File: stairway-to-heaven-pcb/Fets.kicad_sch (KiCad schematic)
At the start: 7 parts, among them J14 Conn_01x04_Male, Q40 FDN337N, Q41 FDN337N, Q42 FDN337N

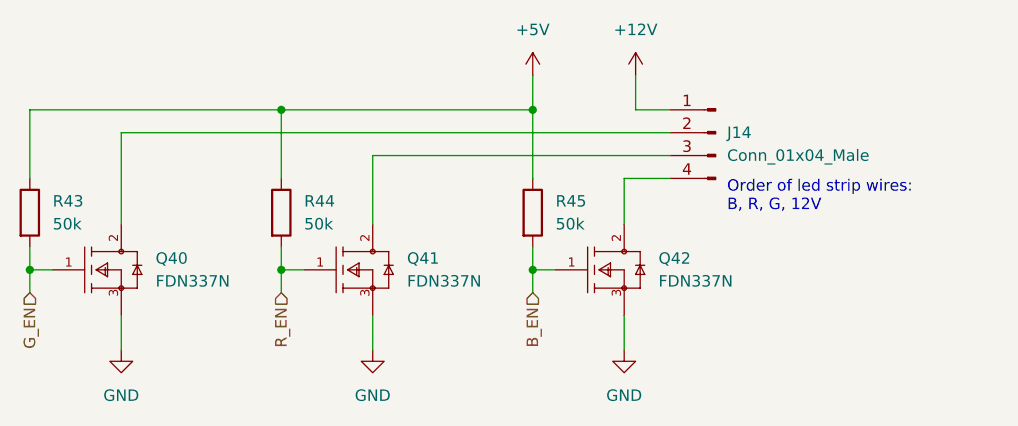
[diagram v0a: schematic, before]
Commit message: Add sensor drawing
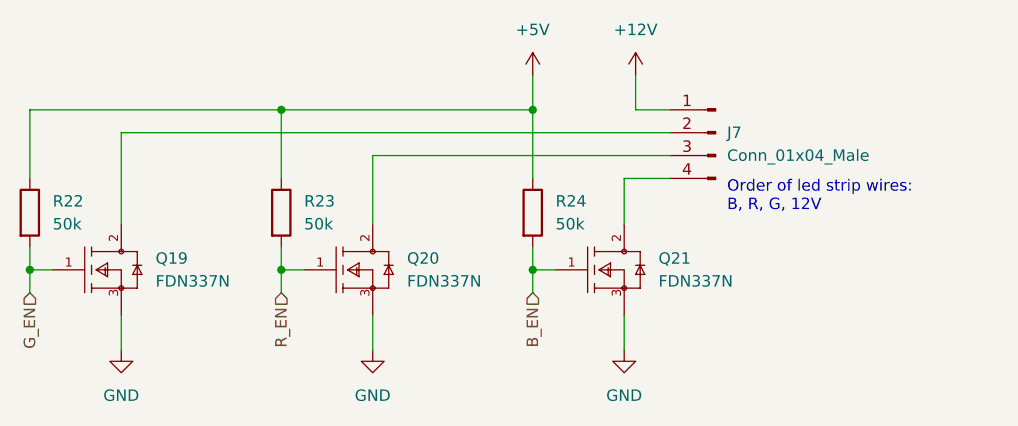
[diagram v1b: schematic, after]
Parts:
- renumbered J14 to J7, Q40 to Q19, Q41 to Q20, Q42 to Q21, R43 to R22, R44 to R23, R45 to R24
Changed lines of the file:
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@@
   (symbol (lib_id "Device:R") (at 96.52 99.06 0)
     (in_bom yes) (on_board yes) (fields_autoplaced)
-    (property "Reference" "R43" (id 0) (at 99.06 97.7899 0)
+    (property "Reference" "R22" (id 0) (at 99.06 97.7899 0)
       (effects (font (size 1.27 1.27)) (justify left))
     )
@@
   (symbol (lib_id "power:GND") (at 162.56 114.3 0)
     (in_bom yes) (on_board yes) (fields_autoplaced)
-    (property "Reference" "#PWR0157" (id 0) (at 162.56 120.65 0)
+    (property "Reference" "#PWR0129" (id 0) (at 162.56 120.65 0)
       (effects (font (size 1.27 1.27)) hide)
     )
@@
   (symbol (lib_id "FDN337N:FDN337N") (at 96.52 105.41 0)
     (in_bom yes) (on_board yes) (fields_autoplaced)
-    (property "Reference" "Q40" (id 0) (at 110.49 104.1399 0)
+    (property "Reference" "Q19" (id 0) (at 110.49 104.1399 0)
       (effects (font (size 1.27 1.27)) (justify left))
     )
@@
   (symbol (lib_id "FDN337N:FDN337N") (at 152.4 105.41 0)
     (in_bom yes) (on_board yes) (fields_autoplaced)
-    (property "Reference" "Q42" (id 0) (at 166.37 104.1399 0)
+    (property "Reference" "Q21" (id 0) (at 166.37 104.1399 0)
       (effects (font (size 1.27 1.27)) (justify left))
     )
@@
   (symbol (lib_id "power:GND") (at 134.62 114.3 0)
     (in_bom yes) (on_board yes) (fields_autoplaced)
-    (property "Reference" "#PWR0155" (id 0) (at 134.62 120.65 0)
+    (property "Reference" "#PWR0127" (id 0) (at 134.62 120.65 0)
       (effects (font (size 1.27 1.27)) hide)
     )
@@
   (symbol (lib_id "Connector:Conn_01x04_Male") (at 172.72 90.17 0) (mirror y)
     (in_bom yes) (on_board yes) (fields_autoplaced)
-    (property "Reference" "J14" (id 0) (at 173.99 90.1699 0)
+    (property "Reference" "J7" (id 0) (at 173.99 90.1699 0)
       (effects (font (size 1.27 1.27)) (justify right))
     )
@@
   (symbol (lib_id "FDN337N:FDN337N") (at 124.46 105.41 0)
     (in_bom yes) (on_board yes) (fields_autoplaced)
-    (property "Reference" "Q41" (id 0) (at 138.43 104.1399 0)
+    (property "Reference" "Q20" (id 0) (at 138.43 104.1399 0)
       (effects (font (size 1.27 1.27)) (justify left))
     )
@@
   (symbol (lib_id "power:+5V") (at 152.4 83.82 0)
     (in_bom yes) (on_board yes) (fields_autoplaced)
-    (property "Reference" "#PWR0179" (id 0) (at 152.4 87.63 0)
+    (property "Reference" "#PWR0172" (id 0) (at 152.4 87.63 0)
       (effects (font (size 1.27 1.27)) hide)
     )
@@
   (symbol (lib_id "power:GND") (at 106.68 114.3 0)
     (in_bom yes) (on_board yes) (fields_autoplaced)
-    (property "Reference" "#PWR0156" (id 0) (at 106.68 120.65 0)
+    (property "Reference" "#PWR0128" (id 0) (at 106.68 120.65 0)
       (effects (font (size 1.27 1.27)) hide)
     )
@@
   (symbol (lib_id "power:+12V") (at 163.83 83.82 0)
     (in_bom yes) (on_board yes) (fields_autoplaced)
-    (property "Reference" "#PWR0158" (id 0) (at 163.83 87.63 0)
+    (property "Reference" "#PWR0130" (id 0) (at 163.83 87.63 0)
       (effects (font (size 1.27 1.27)) hide)
     )
@@
   (symbol (lib_id "Device:R") (at 152.4 99.06 0)
     (in_bom yes) (on_board yes) (fields_autoplaced)
-    (property "Reference" "R45" (id 0) (at 154.94 97.7899 0)
+    (property "Reference" "R24" (id 0) (at 154.94 97.7899 0)
       (effects (font (size 1.27 1.27)) (justify left))
     )
@@
   (symbol (lib_id "Device:R") (at 124.46 99.06 0)
     (in_bom yes) (on_board yes) (fields_autoplaced)
-    (property "Reference" "R44" (id 0) (at 127 97.7899 0)
-      (effects (font (size 1.27 1.27)) (justify left))
-    )
+    (property "Reference" "R23" (id 0) (at 127 97.7899 0)
+      (effects (font (size 1.27 1.27)) (justify left))
+    )

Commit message: Add terminal for sensors
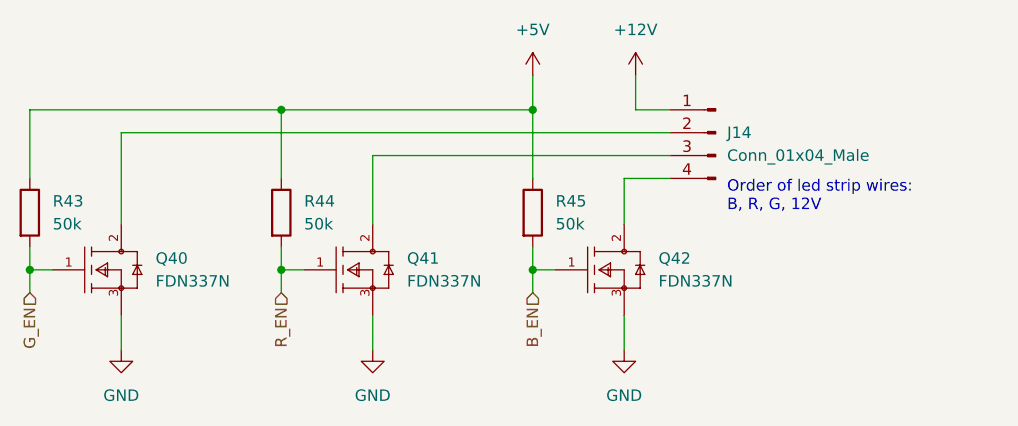
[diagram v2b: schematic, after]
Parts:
- renumbered J7 to J14, Q19 to Q40, Q20 to Q41, Q21 to Q42, R22 to R43, R23 to R44, R24 to R45
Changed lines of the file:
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@@
   (symbol (lib_id "Device:R") (at 96.52 99.06 0)
     (in_bom yes) (on_board yes) (fields_autoplaced)
-    (property "Reference" "R22" (id 0) (at 99.06 97.7899 0)
+    (property "Reference" "R43" (id 0) (at 99.06 97.7899 0)
       (effects (font (size 1.27 1.27)) (justify left))
     )
@@
   (symbol (lib_id "power:GND") (at 162.56 114.3 0)
     (in_bom yes) (on_board yes) (fields_autoplaced)
-    (property "Reference" "#PWR0129" (id 0) (at 162.56 120.65 0)
+    (property "Reference" "#PWR0157" (id 0) (at 162.56 120.65 0)
       (effects (font (size 1.27 1.27)) hide)
     )
@@
   (symbol (lib_id "FDN337N:FDN337N") (at 96.52 105.41 0)
     (in_bom yes) (on_board yes) (fields_autoplaced)
-    (property "Reference" "Q19" (id 0) (at 110.49 104.1399 0)
+    (property "Reference" "Q40" (id 0) (at 110.49 104.1399 0)
       (effects (font (size 1.27 1.27)) (justify left))
     )
@@
   (symbol (lib_id "FDN337N:FDN337N") (at 152.4 105.41 0)
     (in_bom yes) (on_board yes) (fields_autoplaced)
-    (property "Reference" "Q21" (id 0) (at 166.37 104.1399 0)
+    (property "Reference" "Q42" (id 0) (at 166.37 104.1399 0)
       (effects (font (size 1.27 1.27)) (justify left))
     )
@@
   (symbol (lib_id "power:GND") (at 134.62 114.3 0)
     (in_bom yes) (on_board yes) (fields_autoplaced)
-    (property "Reference" "#PWR0127" (id 0) (at 134.62 120.65 0)
+    (property "Reference" "#PWR0155" (id 0) (at 134.62 120.65 0)
       (effects (font (size 1.27 1.27)) hide)
     )
@@
   (symbol (lib_id "Connector:Conn_01x04_Male") (at 172.72 90.17 0) (mirror y)
     (in_bom yes) (on_board yes) (fields_autoplaced)
-    (property "Reference" "J7" (id 0) (at 173.99 90.1699 0)
+    (property "Reference" "J14" (id 0) (at 173.99 90.1699 0)
       (effects (font (size 1.27 1.27)) (justify right))
     )
@@
   (symbol (lib_id "FDN337N:FDN337N") (at 124.46 105.41 0)
     (in_bom yes) (on_board yes) (fields_autoplaced)
-    (property "Reference" "Q20" (id 0) (at 138.43 104.1399 0)
+    (property "Reference" "Q41" (id 0) (at 138.43 104.1399 0)
       (effects (font (size 1.27 1.27)) (justify left))
     )
@@
   (symbol (lib_id "power:+5V") (at 152.4 83.82 0)
     (in_bom yes) (on_board yes) (fields_autoplaced)
-    (property "Reference" "#PWR0172" (id 0) (at 152.4 87.63 0)
+    (property "Reference" "#PWR0179" (id 0) (at 152.4 87.63 0)
       (effects (font (size 1.27 1.27)) hide)
     )
@@
   (symbol (lib_id "power:GND") (at 106.68 114.3 0)
     (in_bom yes) (on_board yes) (fields_autoplaced)
-    (property "Reference" "#PWR0128" (id 0) (at 106.68 120.65 0)
+    (property "Reference" "#PWR0156" (id 0) (at 106.68 120.65 0)
       (effects (font (size 1.27 1.27)) hide)
     )
@@
   (symbol (lib_id "power:+12V") (at 163.83 83.82 0)
     (in_bom yes) (on_board yes) (fields_autoplaced)
-    (property "Reference" "#PWR0130" (id 0) (at 163.83 87.63 0)
+    (property "Reference" "#PWR0158" (id 0) (at 163.83 87.63 0)
       (effects (font (size 1.27 1.27)) hide)
     )
@@
   (symbol (lib_id "Device:R") (at 152.4 99.06 0)
     (in_bom yes) (on_board yes) (fields_autoplaced)
-    (property "Reference" "R24" (id 0) (at 154.94 97.7899 0)
+    (property "Reference" "R45" (id 0) (at 154.94 97.7899 0)
       (effects (font (size 1.27 1.27)) (justify left))
     )
@@
   (symbol (lib_id "Device:R") (at 124.46 99.06 0)
     (in_bom yes) (on_board yes) (fields_autoplaced)
-    (property "Reference" "R23" (id 0) (at 127 97.7899 0)
-      (effects (font (size 1.27 1.27)) (justify left))
-    )
+    (property "Reference" "R44" (id 0) (at 127 97.7899 0)
+      (effects (font (size 1.27 1.27)) (justify left))
+    )

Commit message: Add pdf prints for infinity-table, advent-calendar and stairway-to-heaven.
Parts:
- renumbered J14 to J1, Q40 to Q1, Q41 to Q2, Q42 to Q3, R43 to R4, R44 to R5, R45 to R6
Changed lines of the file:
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@@
     (effects (font (size 1.27 1.27)) (justify right))
   )
-  (symbol (lib_id "Device:R") (at 96.52 99.06 0)
-    (in_bom yes) (on_board yes) (fields_autoplaced)
-    (property "Reference" "R43" (id 0) (at 99.06 97.7899 0)
+  (symbol (lib_id "Device:R") (at 96.52 99.06 0) (unit 1)
+    (in_bom yes) (on_board yes) (fields_autoplaced)
+    (property "Reference" "R4" (id 0) (at 99.06 97.7899 0)
       (effects (font (size 1.27 1.27)) (justify left))
     )
@@
     (pin "2")
   )
-  (symbol (lib_id "power:GND") (at 162.56 114.3 0)
-    (in_bom yes) (on_board yes) (fields_autoplaced)
-    (property "Reference" "#PWR0157" (id 0) (at 162.56 120.65 0)
+  (symbol (lib_id "power:GND") (at 162.56 114.3 0) (unit 1)
+    (in_bom yes) (on_board yes) (fields_autoplaced)
+    (property "Reference" "#PWR0103" (id 0) (at 162.56 120.65 0)
       (effects (font (size 1.27 1.27)) hide)
     )
@@
     (pin "1")
   )
-  (symbol (lib_id "FDN337N:FDN337N") (at 96.52 105.41 0)
-    (in_bom yes) (on_board yes) (fields_autoplaced)
-    (property "Reference" "Q40" (id 0) (at 110.49 104.1399 0)
+  (symbol (lib_id "FDN337N:FDN337N") (at 96.52 105.41 0) (unit 1)
+    (in_bom yes) (on_board yes) (fields_autoplaced)
+    (property "Reference" "Q1" (id 0) (at 110.49 104.1399 0)
       (effects (font (size 1.27 1.27)) (justify left))
     )
@@
     (pin "3")
   )
-  (symbol (lib_id "FDN337N:FDN337N") (at 152.4 105.41 0)
-    (in_bom yes) (on_board yes) (fields_autoplaced)
-    (property "Reference" "Q42" (id 0) (at 166.37 104.1399 0)
+  (symbol (lib_id "FDN337N:FDN337N") (at 152.4 105.41 0) (unit 1)
+    (in_bom yes) (on_board yes) (fields_autoplaced)
+    (property "Reference" "Q3" (id 0) (at 166.37 104.1399 0)
       (effects (font (size 1.27 1.27)) (justify left))
     )
@@
     (pin "3")
   )
-  (symbol (lib_id "power:GND") (at 134.62 114.3 0)
-    (in_bom yes) (on_board yes) (fields_autoplaced)
-    (property "Reference" "#PWR0155" (id 0) (at 134.62 120.65 0)
+  (symbol (lib_id "power:GND") (at 134.62 114.3 0) (unit 1)
+    (in_bom yes) (on_board yes) (fields_autoplaced)
+    (property "Reference" "#PWR0105" (id 0) (at 134.62 120.65 0)
       (effects (font (size 1.27 1.27)) hide)
     )
@@
     (pin "1")
   )
-  (symbol (lib_id "Connector:Conn_01x04_Male") (at 172.72 90.17 0) (mirror y)
-    (in_bom yes) (on_board yes) (fields_autoplaced)
-    (property "Reference" "J14" (id 0) (at 173.99 90.1699 0)
+  (symbol (lib_id "Connector:Conn_01x04_Male") (at 172.72 90.17 0) (mirror y) (unit 1)
+    (in_bom yes) (on_board yes) (fields_autoplaced)
+    (property "Reference" "J1" (id 0) (at 173.99 90.1699 0)
       (effects (font (size 1.27 1.27)) (justify right))
     )
@@
     (pin "4")
   )
-  (symbol (lib_id "FDN337N:FDN337N") (at 124.46 105.41 0)
-    (in_bom yes) (on_board yes) (fields_autoplaced)
-    (property "Reference" "Q41" (id 0) (at 138.43 104.1399 0)
+  (symbol (lib_id "FDN337N:FDN337N") (at 124.46 105.41 0) (unit 1)
+    (in_bom yes) (on_board yes) (fields_autoplaced)
+    (property "Reference" "Q2" (id 0) (at 138.43 104.1399 0)
       (effects (font (size 1.27 1.27)) (justify left))
     )
@@
     (pin "3")
   )
-  (symbol (lib_id "power:+5V") (at 152.4 83.82 0)
-    (in_bom yes) (on_board yes) (fields_autoplaced)
-    (property "Reference" "#PWR0179" (id 0) (at 152.4 87.63 0)
+  (symbol (lib_id "power:+5V") (at 152.4 83.82 0) (unit 1)
+    (in_bom yes) (on_board yes) (fields_autoplaced)
+    (property "Reference" "#PWR0166" (id 0) (at 152.4 87.63 0)
       (effects (font (size 1.27 1.27)) hide)
     )
@@
     (pin "1")
   )
-  (symbol (lib_id "power:GND") (at 106.68 114.3 0)
-    (in_bom yes) (on_board yes) (fields_autoplaced)
-    (property "Reference" "#PWR0156" (id 0) (at 106.68 120.65 0)
+  (symbol (lib_id "power:GND") (at 106.68 114.3 0) (unit 1)
+    (in_bom yes) (on_board yes) (fields_autoplaced)
+    (property "Reference" "#PWR0106" (id 0) (at 106.68 120.65 0)
       (effects (font (size 1.27 1.27)) hide)
     )
@@
     (pin "1")
   )
-  (symbol (lib_id "power:+12V") (at 163.83 83.82 0)
-    (in_bom yes) (on_board yes) (fields_autoplaced)
-    (property "Reference" "#PWR0158" (id 0) (at 163.83 87.63 0)
+  (symbol (lib_id "power:+12V") (at 163.83 83.82 0) (unit 1)
+    (in_bom yes) (on_board yes) (fields_autoplaced)
+    (property "Reference" "#PWR0104" (id 0) (at 163.83 87.63 0)
       (effects (font (size 1.27 1.27)) hide)
     )
@@
     (pin "1")
   )
-  (symbol (lib_id "Device:R") (at 152.4 99.06 0)
-    (in_bom yes) (on_board yes) (fields_autoplaced)
-    (property "Reference" "R45" (id 0) (at 154.94 97.7899 0)
+  (symbol (lib_id "Device:R") (at 152.4 99.06 0) (unit 1)
+    (in_bom yes) (on_board yes) (fields_autoplaced)
+    (property "Reference" "R6" (id 0) (at 154.94 97.7899 0)
       (effects (font (size 1.27 1.27)) (justify left))
     )
@@
     (pin "2")
   )
-  (symbol (lib_id "Device:R") (at 124.46 99.06 0)
-    (in_bom yes) (on_board yes) (fields_autoplaced)
-    (property "Reference" "R44" (id 0) (at 127 97.7899 0)
-      (effects (font (size 1.27 1.27)) (justify left))
-    )
+  (symbol (lib_id "Device:R") (at 124.46 99.06 0) (unit 1)
+    (in_bom yes) (on_board yes) (fields_autoplaced)
+    (property "Reference" "R5" (id 0) (at 127 97.7899 0)
+      (effects (font (size 1.27 1.27)) (justify left))
+    )
